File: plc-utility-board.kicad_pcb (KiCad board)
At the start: 2 copper layers, 117 parts, among them J1 Screw_Terminal_01x02, J10 Screw_Terminal_01x03, J11 Screw_Terminal_01x02, J2 Screw_Terminal_01x08, J3 Screw_Terminal_01x04, J4 Screw_Terminal_01x08, J5 Screw_Terminal_01x04, J6 Conn_01x03_Male, J7 Conn_01x03_Male, J8 Screw_Terminal_01x03, J9 Screw_Terminal_01x02, Q1 2N7002, Q10 2N7002, Q11 2N7002, Q12 2N7002, Q13 FDV304, Q14 2N7002, Q15 2N7002, Q16 2N7002, Q2 2N7002, Q3 Q_PMOS_GSD, Q4 Q_PMOS_GSD, Q5 2N7002, Q6 2N7002, Q7 Q_PMOS_GSD, Q8 Q_PMOS_GSD, Q9 FDV304, SW1 SW_Push, SW2 SW_Push, SW3 SW_Push, SW4 SW_Push, SW5 SW_Push, SW6 SW_Push, U1 L78L33_SOT89, U2 DRV8840, U3 DRV8840

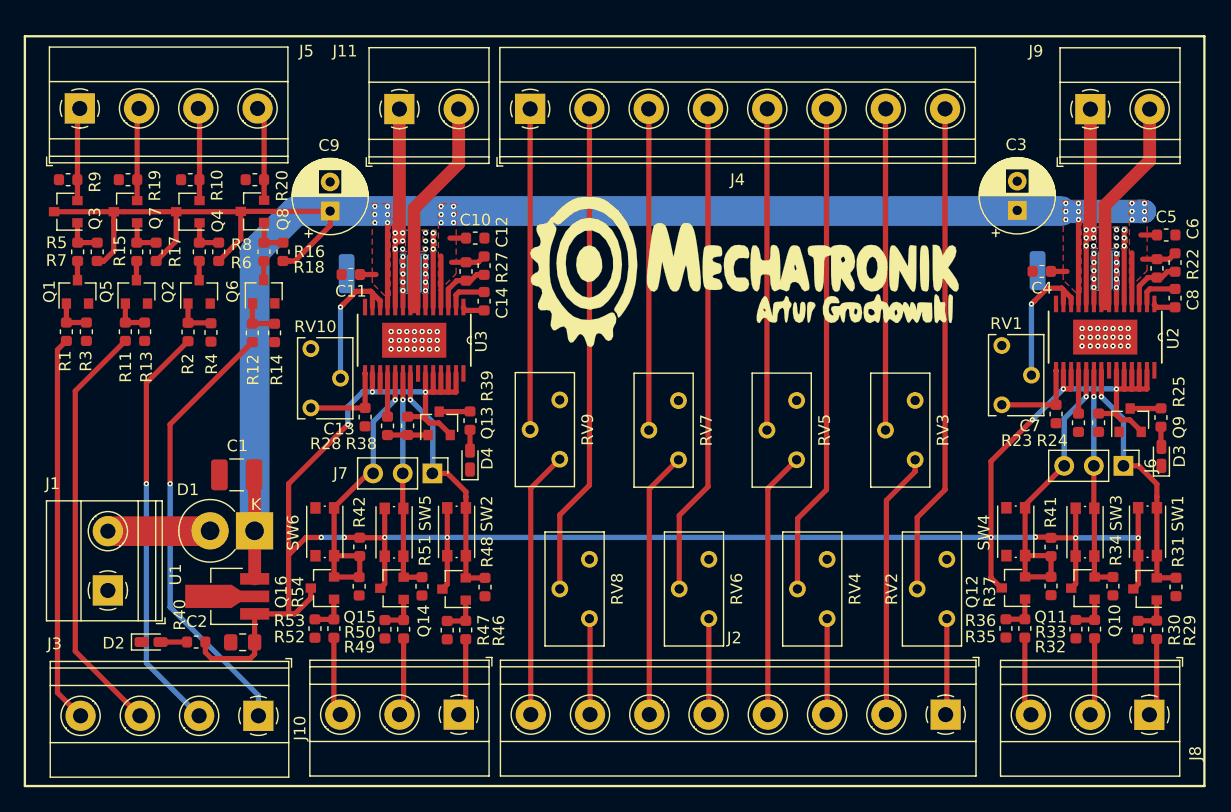
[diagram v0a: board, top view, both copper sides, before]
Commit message: Added elapsed 3D models for components
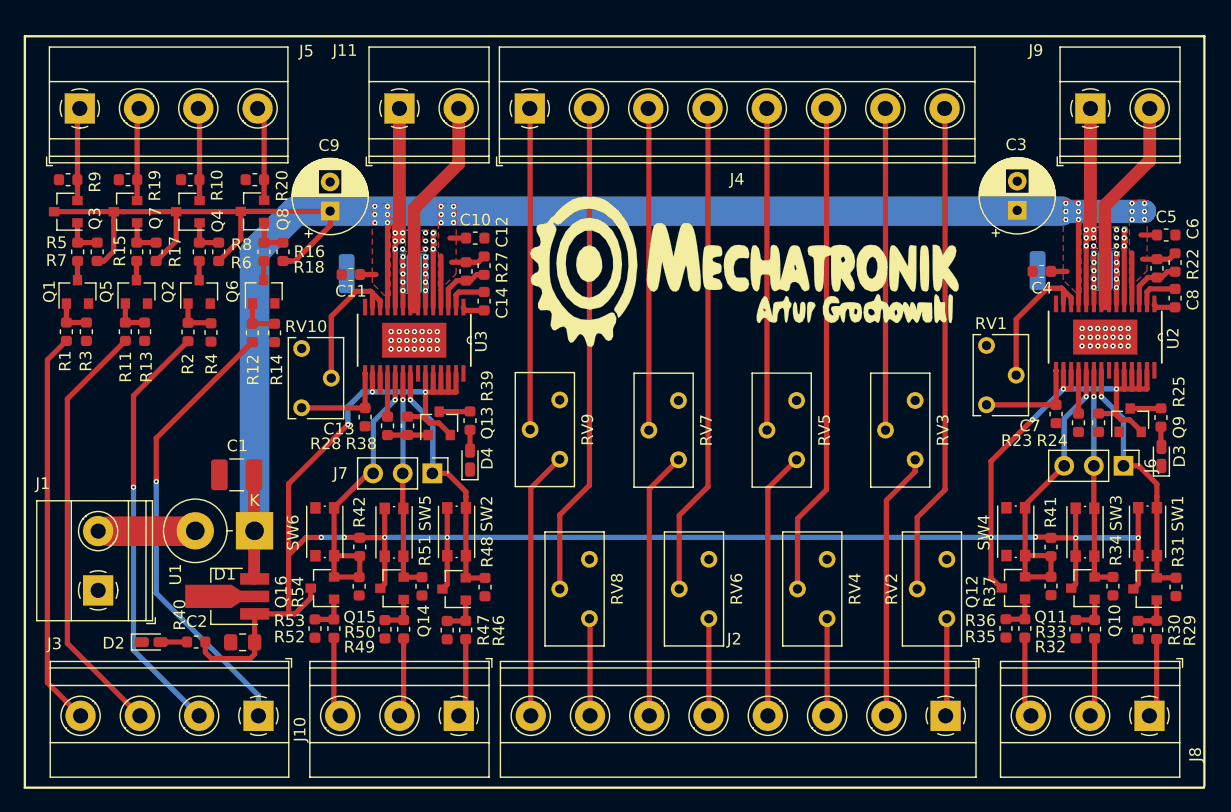
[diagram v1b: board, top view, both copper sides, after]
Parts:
- D1: footprint Diode_THT:D_DO-201AD_P3.81mm_Vertical_KathodeUp -> Diode_THT:D_DO-201AD_P5.08mm_Vertical_KathodeUp
- moved RV1 1.31 mm to (182.8, 89.2)
- moved J1 0.83 mm to (106.6, 110.2)
- moved RV10 0.79 mm to (124.0, 89.5)
- moved J10 0.10 mm to (137.5, 121.0)
- moved J2 0.10 mm to (179.2, 121.0)
- moved J8 0.09 mm to (196.7, 121.0)
- moved J9 0.06 mm to (191.7, 68.9)
- moved J11 0.05 mm to (132.4, 68.9)
- moved J4 0.05 mm to (143.6, 68.9)
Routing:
- net Net-(C7-Pad1): track 7.62 -> 8.93 mm
- net /Power section/VIN: track 8.78 -> 7.51 mm
- net /ttl-to-plc/IN4: track 38.1 -> 39.1 mm
- net /ttl-to-plc/IN3: track 35.5 -> 36.4 mm
- net Net-(C13-Pad1): track 7.62 -> 8.42 mm
- net /ttl-to-plc/IN1: track 33.3 -> 34.0 mm
- net /ttl-to-plc/IN2: track 36.2 -> 36.8 mm

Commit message: Added switch for selecting Low/High power motor. Added thermal pads around motor controllers.
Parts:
- removed the G*** at (145.3, 77.7)
- removed the G*** at (161.9, 82.8)
- added G***: LOGO, plc-utility-board:logo, F.Cu at (161.4, 83.1)
- added SW7: SW_DIP_x01, mylib:CHS01TB, F.Cu at (198.8, 97.1)
- added SW8: SW_DIP_x01, mylib:CHS01TB, F.Cu at (140.2, 97.0)
- R37, R54: value 10k -> 4.7k
- moved R25 4.13 mm to (196.3, 99.3)
- moved R39 3.99 mm to (137.7, 99.6)
- moved D3 3.17 mm to (194.6, 99.3), turned to 270 degrees
- moved J6 2.61 mm to (191.9, 99.5)
- moved D4 2.47 mm to (136.1, 99.6), turned to 270 degrees
- moved J7 1.91 mm to (133.3, 100.2)
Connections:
- U2 pad 26: /Motor1 3V3 <- PLC/3V3 -> Net-(SW7-Pad2)
- U2 pad 27: /Motor1 3V3 <- PLC/3V3 -> Net-(SW7-Pad2)
- U3 pad 26: /Motor1 3V3 <- PLC/3V3 -> Net-(SW8-Pad2)
- U3 pad 27: /Motor1 3V3 <- PLC/3V3 -> Net-(SW8-Pad2)
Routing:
- net Net-(SW8-Pad2): track 0.00 -> 6.62 mm
- net Net-(SW7-Pad2): track 0.00 -> 6.19 mm
- net /Motor1 3V3 <- PLC/3V3: track 210.6 -> 214.4 mm, vias 14 -> 16
- net Net-(Q9-Pad3): track 2.65 -> 6.40 mm
- net Net-(Q9-Pad1): track 0.00 -> 3.48 mm
- net Net-(Q13-Pad3): track 2.65 -> 5.88 mm
- net /Motor1 3V3 <- PLC/OUT2: track 19.3 -> 22.3 mm
- net /Motor2 3V3 <- PLC/OUT2: track 18.9 -> 21.4 mm
- net /Motor1 driver/ENABLE: track 22.2 -> 24.4 mm
- net /Motor2 driver/ENABLE: track 21.6 -> 23.6 mm
- net Net-(RV1-Pad2): track 12.6 -> 13.6 mm
- net Net-(RV10-Pad2): track 12.3 -> 13.1 mm
- net GND: vias 42 -> 150

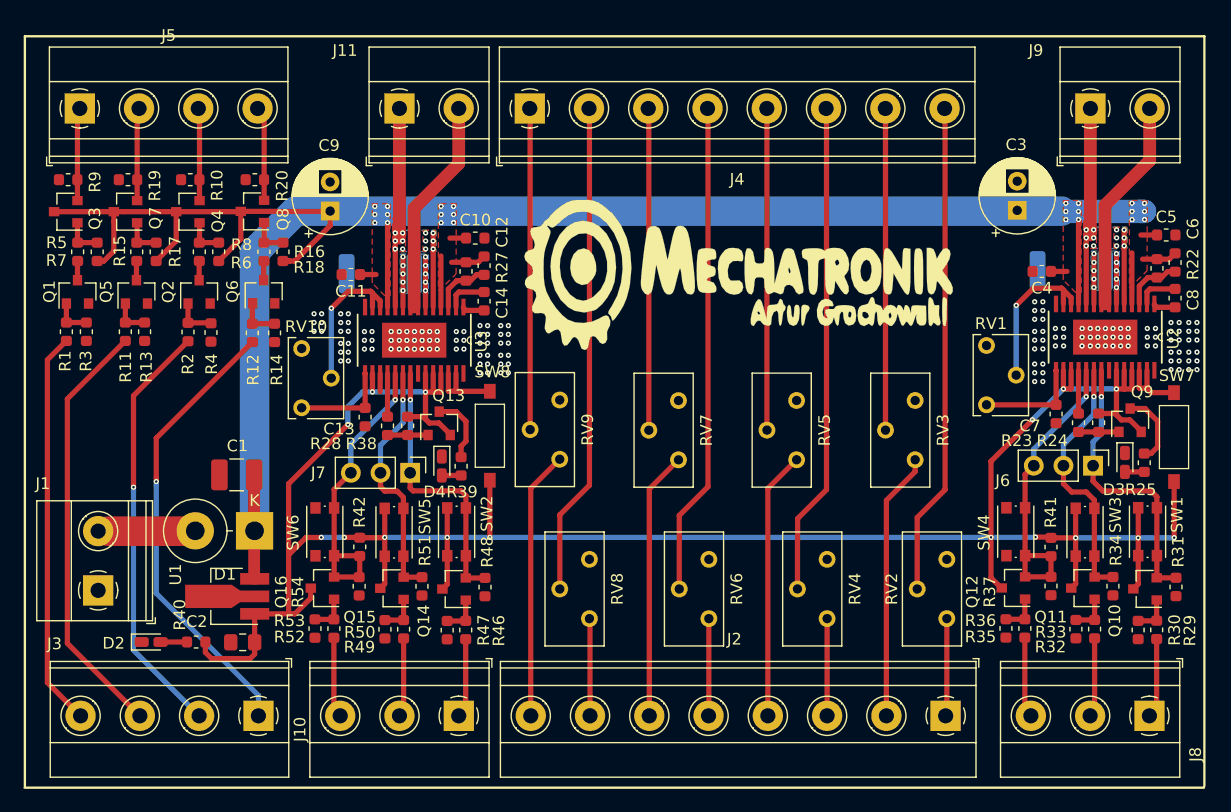
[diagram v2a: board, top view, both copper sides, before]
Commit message: Added GND zones. Changed priority of motor controllers voltage zones to 1. Added labels to terminal blocks
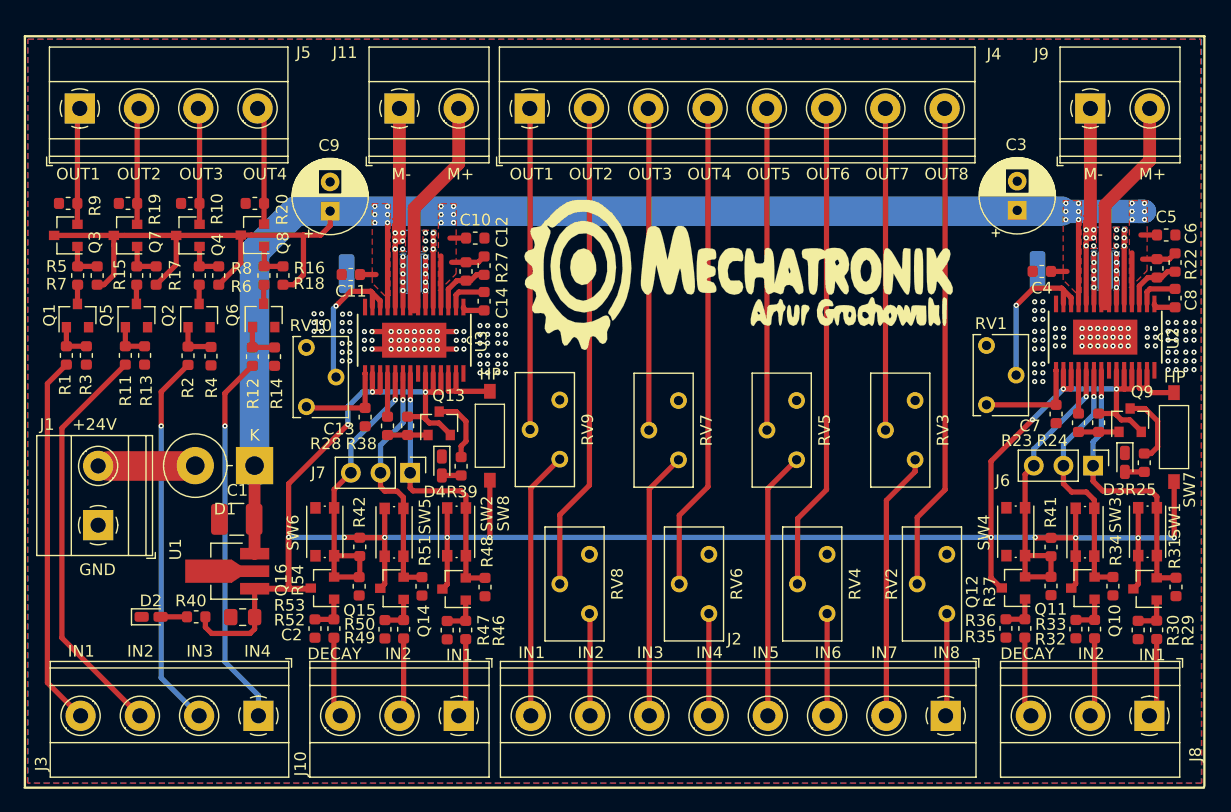
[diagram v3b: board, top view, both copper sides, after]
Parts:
- moved J1 5.59 mm to (106.6, 104.6)
- moved D1 5.59 mm to (120.0, 99.5)
- moved C1 3.81 mm to (118.5, 104.1)
- moved D2 2.16 mm to (111.2, 112.5)
- moved R40 2.16 mm to (115.0, 112.5)
- moved U1 2.16 mm to (118.0, 108.6)
- moved C2 2.16 mm to (119.0, 112.5)
- moved R12 2.03 mm to (119.8, 90.2)
- moved R14 2.03 mm to (121.7, 90.2)
- moved R4 2.03 mm to (116.3, 90.2)
- moved Q1 2.03 mm to (104.8, 86.7)
- moved Q2 2.03 mm to (115.3, 86.7)
- moved Q3 2.03 mm to (103.8, 79.8)
- moved Q4 2.03 mm to (114.3, 79.8)
- moved Q5 2.03 mm to (109.9, 86.7)
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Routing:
- net GND: track 0.00 -> 8.83 mm
- net /ttl-to-plc/IN4: track 39.1 -> 32.2 mm
- net /Power section/24V: track 191.2 -> 185.3 mm
- net /ttl-to-plc/IN3: track 36.4 -> 32.4 mm
- net /Motor1 3V3 <- PLC/3V3: track 214.4 -> 217.9 mm
- net /ttl-to-plc/OUT4: track 8.10 -> 10.1 mm
- net /ttl-to-plc/OUT3: track 7.94 -> 9.98 mm
- net /ttl-to-plc/OUT2: track 7.97 -> 10.00 mm
- net /ttl-to-plc/OUT1: track 7.98 -> 10.0 mm
- net /ttl-to-plc/IN1: track 34.0 -> 32.0 mm
- net /ttl-to-plc/IN2: track 36.8 -> 35.1 mm
- added copper zone on B.Cu, net GND
- added copper zone on F.Cu, net GND
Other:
- board text added: "+24V"
- board text added: "DECAY"
- board text added: "GND"
- board text added: "HP"
- board text added: "IN1"
- board text added: "IN2"
- board text added: "IN3"
- board text added: "IN4"
- board text added: "IN5"
- board text added: "IN6"
- board text added: "IN7"
- board text added: "IN8"
- board text added: "M+"
- board text added: "M-"
- board text added: "OUT1"
- board text added: "OUT2"
- board text added: "OUT3"
- board text added: "OUT4"
- board text added: "OUT5"
- board text added: "OUT6"
- board text added: "OUT7"
- board text added: "OUT8"

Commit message: Altered connections of button switch to decay pin from GND to 3.3V (also removed unnecessary resistor)
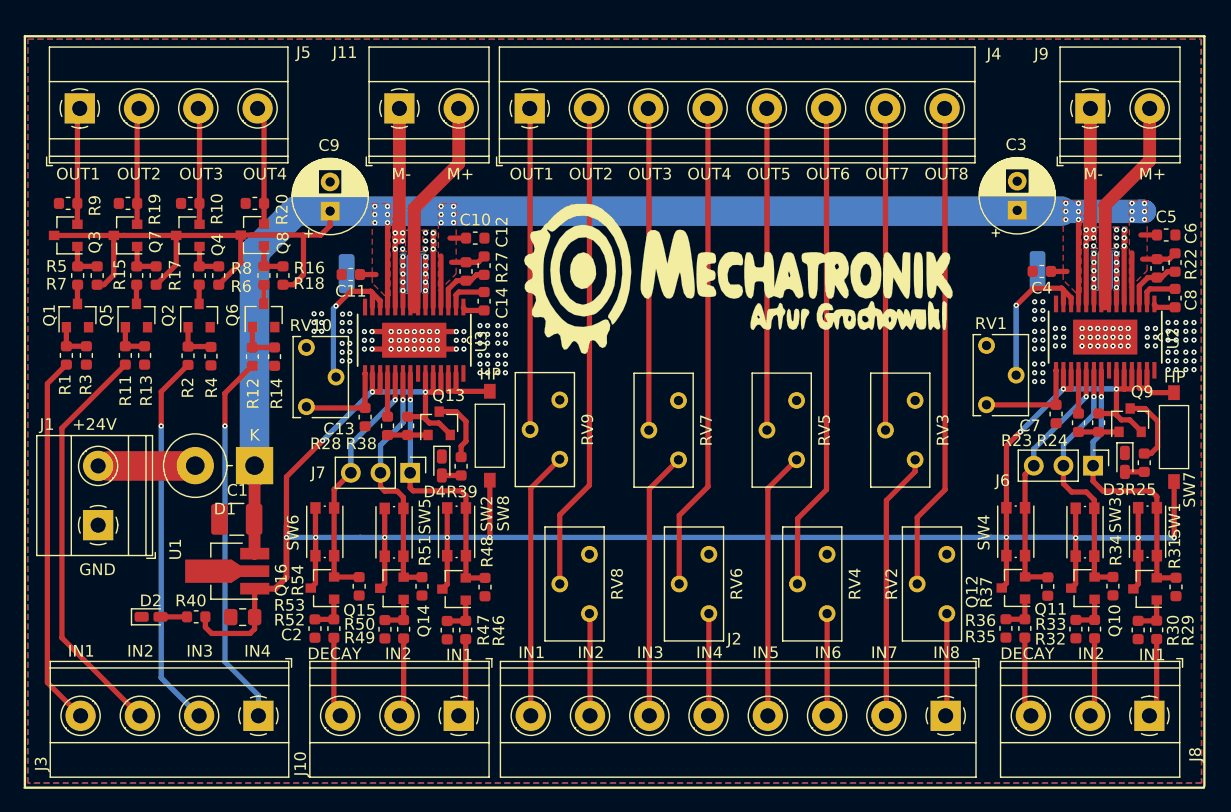
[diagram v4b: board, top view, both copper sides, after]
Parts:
- removed R41, R42: 33k, Resistor_SMD:R_0603_1608Metric
- R37, R54: value 4.7k -> 10k
- moved G*** 0.34 mm to (161.4, 83.4)
- moved R37 0.28 mm to (188.0, 109.9)
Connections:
- SW4 pad 2: GND -> /Motor1 3V3 <- PLC/3V3
- SW6 pad 2: GND -> /Motor1 3V3 <- PLC/3V3
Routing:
- net /Motor1 driver/DECAY: track 26.4 -> 22.1 mm
- net /Motor2 driver/DECAY: track 25.8 -> 21.8 mm
- net /Motor1 3V3 <- PLC/3V3: track 217.9 -> 214.4 mm, vias 16 -> 15

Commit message: Added mounting holes for M3 screws. Performed DRC check.
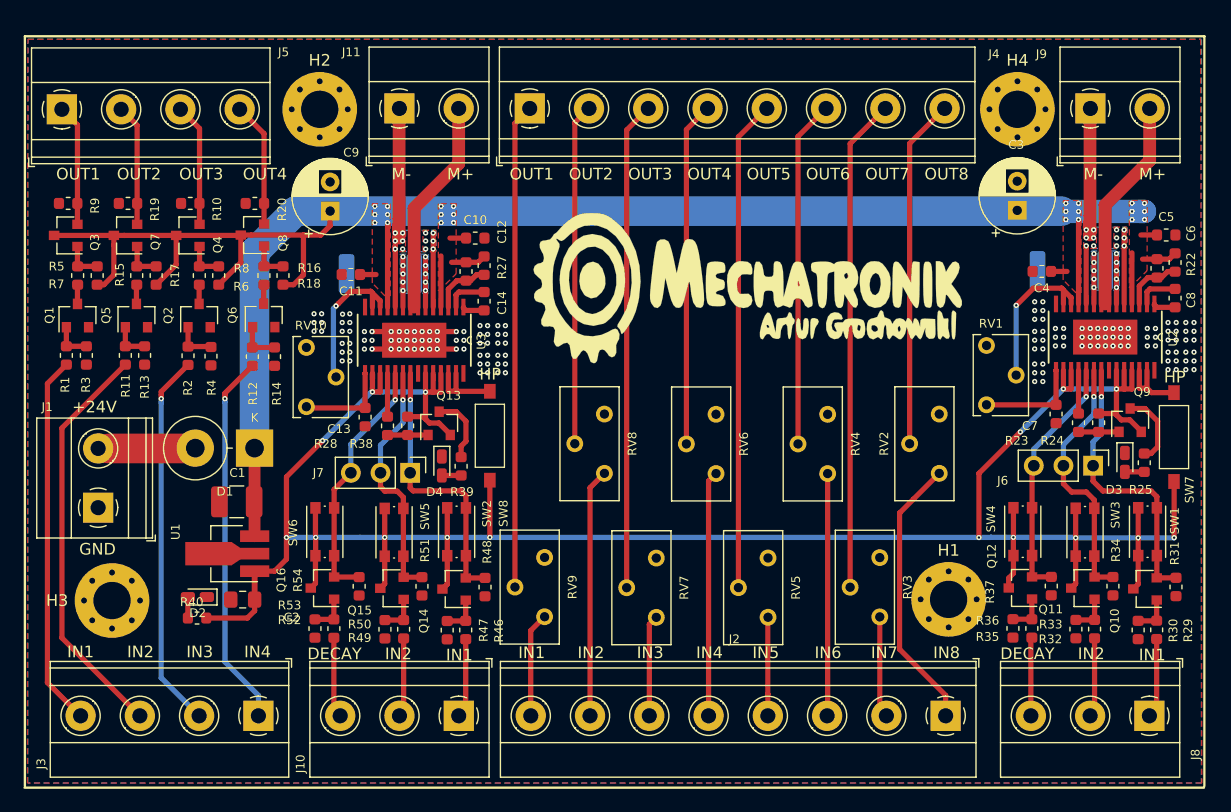
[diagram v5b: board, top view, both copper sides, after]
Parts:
- added H1: MountingHole, MountingHole:MountingHole_3.2mm_M3_Pad_Via, F.Cu at (179.5, 111.0)
- added H2: MountingHole, MountingHole:MountingHole_3.2mm_M3_Pad_Via, F.Cu at (125.6, 69.0)
- added H3: MountingHole, MountingHole:MountingHole_3.2mm_M3_Pad_Via, F.Cu at (107.8, 111.1)
- added H4: MountingHole, MountingHole:MountingHole_3.2mm_M3_Pad_Via, F.Cu at (185.4, 69.0)
- moved RV3 13.8 mm to (173.6, 112.5)
- moved RV5 13.7 mm to (164.0, 112.5)
- moved RV7 13.6 mm to (154.4, 112.5)
- moved RV9 13.6 mm to (144.9, 112.5)
- moved RV8 12.1 mm to (150.0, 100.2)
- moved RV2 12.0 mm to (178.7, 100.2)
- moved RV6 12.0 mm to (159.6, 100.2)
- moved RV4 12.0 mm to (169.1, 100.2)
- moved D2 4.31 mm to (115.1, 110.8), turned to 180 degrees
- moved J5 1.54 mm to (103.5, 69.0)
- moved C1 1.50 mm to (118.5, 102.6)
- moved C2 1.50 mm to (119.0, 111.0)
- moved D1 1.50 mm to (120.0, 98.0)
- moved J1 1.50 mm to (106.6, 103.1)
- moved U1 1.50 mm to (118.0, 107.1)
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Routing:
- net /plc-to-ttl/IN8: track 8.27 -> 24.0 mm
- net /plc-to-ttl/OUT7: track 27.5 -> 42.3 mm
- net /plc-to-ttl/OUT5: track 27.5 -> 42.1 mm
- net /plc-to-ttl/IN5: track 22.9 -> 8.46 mm
- net /plc-to-ttl/OUT3: track 27.5 -> 41.9 mm
- net /plc-to-ttl/IN3: track 22.9 -> 8.69 mm
- net /plc-to-ttl/OUT1: track 27.5 -> 41.6 mm
- net /plc-to-ttl/IN1: track 22.9 -> 8.98 mm
- net /plc-to-ttl/IN7: track 22.9 -> 9.04 mm
- net /plc-to-ttl/IN2: track 8.25 -> 21.3 mm
- net /plc-to-ttl/OUT2: track 42.2 -> 29.2 mm
- net /plc-to-ttl/IN4: track 8.24 -> 21.1 mm
- net /plc-to-ttl/OUT4: track 42.2 -> 29.5 mm
- net /plc-to-ttl/IN6: track 8.23 -> 20.8 mm
- net /plc-to-ttl/OUT6: track 42.2 -> 29.8 mm
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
